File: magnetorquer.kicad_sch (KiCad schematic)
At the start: 20 parts, among them J2 Conn_01x07_Female, SW1 SW_Push, U1 MSP430FR5994IPN, Y1 Crystal, Y2 DNP

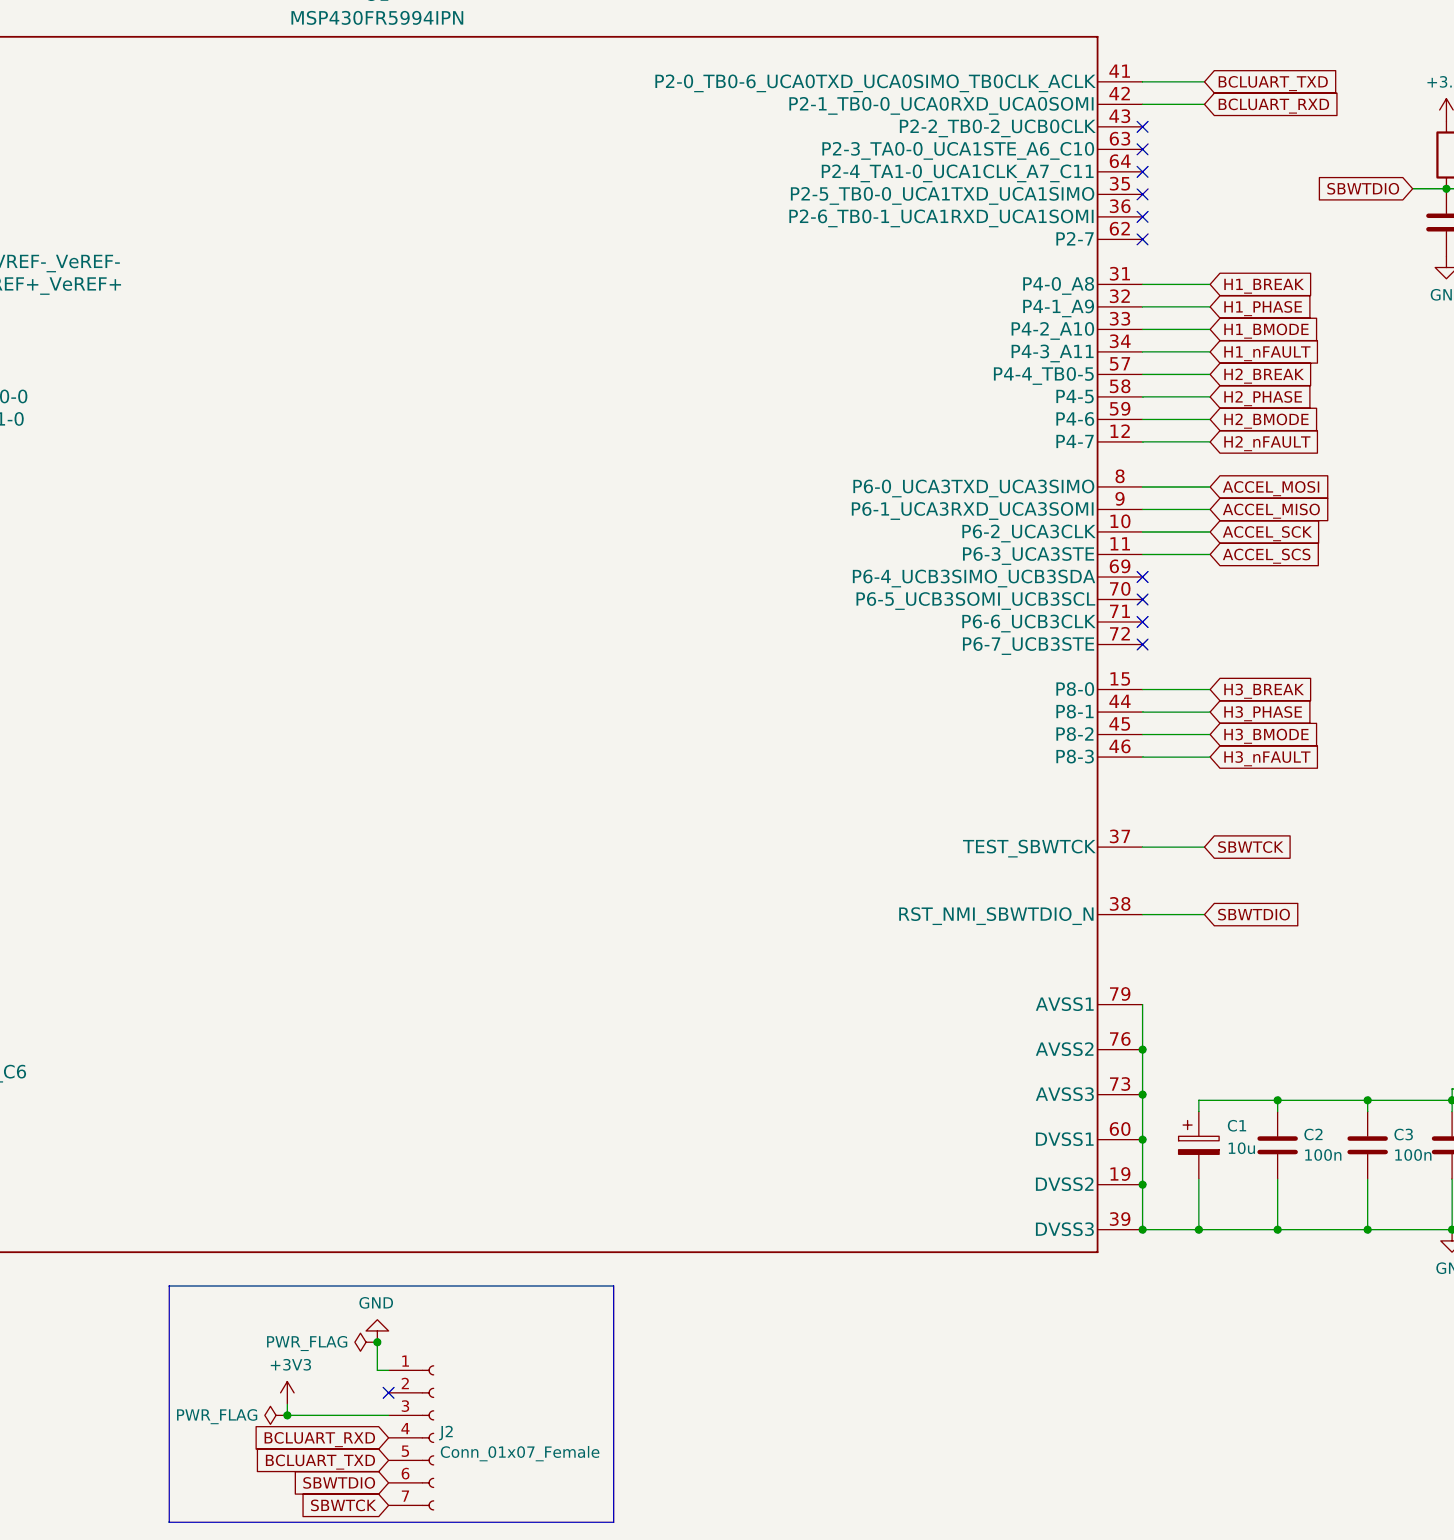
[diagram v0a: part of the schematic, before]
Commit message: schematic update hall sensor
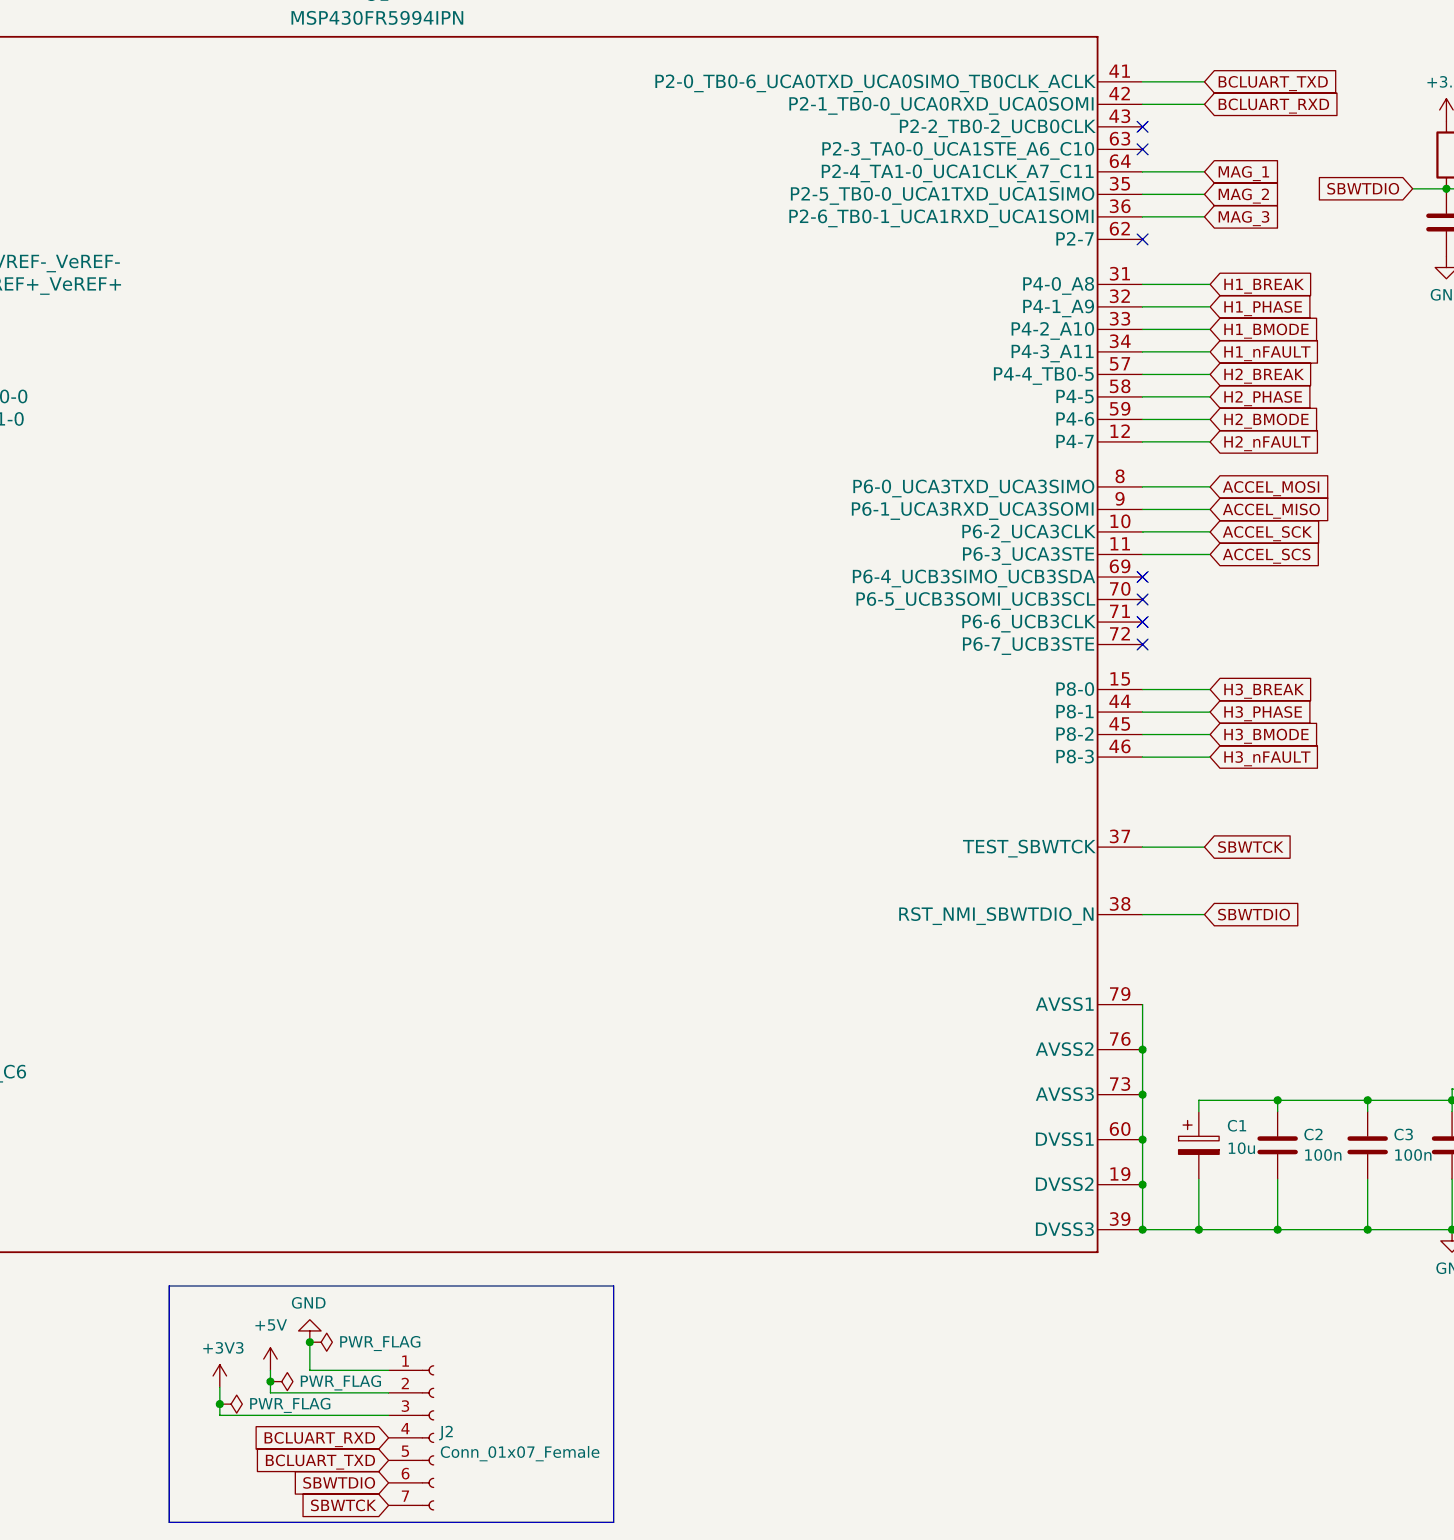
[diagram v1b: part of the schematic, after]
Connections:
- net MAG_2: now reaches U1.35 (P2-5_TB0-0_UCA1TXD_UCA1SIMO)
- net MAG_3: now reaches U1.36 (P2-6_TB0-1_UCA1RXD_UCA1SOMI)
- net MAG_1: now reaches U1.64 (P2-4_TA1-0_UCA1CLK_A7_C11)
- net +5V: now reaches J2.2 (Pin_2)
- no-connect marks 29 -> 25

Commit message: start layout
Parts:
- U1: footprint magnetorque_lib:MSP430FR5994IPM -> magnetorque_lib:MSP430FR5994IPN; symbol magnetorquer-rescue:MSP430FR5994IPN-msp -> msp:MSP430FR5994IPN
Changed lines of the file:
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@@
     )
   )
-  (symbol (lib_id "magnetorquer-rescue:MSP430FR5994IPN-msp") (at 144.145 93.98 0) (unit 1)
+  (symbol (lib_id "msp:MSP430FR5994IPN") (at 144.145 93.98 0) (unit 1)
     (in_bom yes) (on_board yes)
     (property "Reference" "U1" (id 0) (at 144.145 20.6248 0)
@@
       (effects (font (size 1.524 1.524)))
     )
-    (property "Footprint" "magnetorque_lib:MSP430FR5994IPM" (id 2) (at 144.145 95.504 0)
-      (effects (font (size 1.524 1.524)) hide)
+    (property "Footprint" "magnetorque_lib:MSP430FR5994IPN" (id 2) (at 144.145 95.504 0)
+      (effects (font (size 1.524 1.524)))
     )
     (property "Datasheet" "" (id 3) (at 144.145 93.98 0)
@@
     )
     (path "/00000000-0000-0000-0000-00006179e03e/fdcb2037-bdef-4a8f-9927-3cf386350a08"
-      (reference "L1") (unit 1) (value "L_Iron") (footprint "")
+      (reference "L1") (unit 1) (value "L_Iron") (footprint "magnetorque_lib:magnetorquer")
     )
     (path "/00000000-0000-0000-0000-00006179e03e/2085504c-bacb-4d13-8d16-341c091f40b1"
-      (reference "L2") (unit 1) (value "L_Iron") (footprint "")
+      (reference "L2") (unit 1) (value "L_Iron") (footprint "magnetorque_lib:magnetorquer")
     )
     (path "/00000000-0000-0000-0000-00006179e03e/e07af271-de8d-49c5-8d5e-0dfd6ae788f6"
-      (reference "L3") (unit 1) (value "L_Iron") (footprint "")
+      (reference "L3") (unit 1) (value "L_Iron") (footprint "magnetorque_lib:magnetorquer")
     )
     (path "/00000000-0000-0000-0000-00006166ef94"
@@
     )
     (path "/00000000-0000-0000-0000-0000615e437b"
-      (reference "U1") (unit 1) (value "MSP430FR5994IPN") (footprint "magnetorque_lib:MSP430FR5994IPM")
+      (reference "U1") (unit 1) (value "MSP430FR5994IPN") (footprint "magnetorque_lib:MSP430FR5994IPN")
     )
     (path "/00000000-0000-0000-0000-00006179e03e/00000000-0000-0000-0000-0000617b4502"

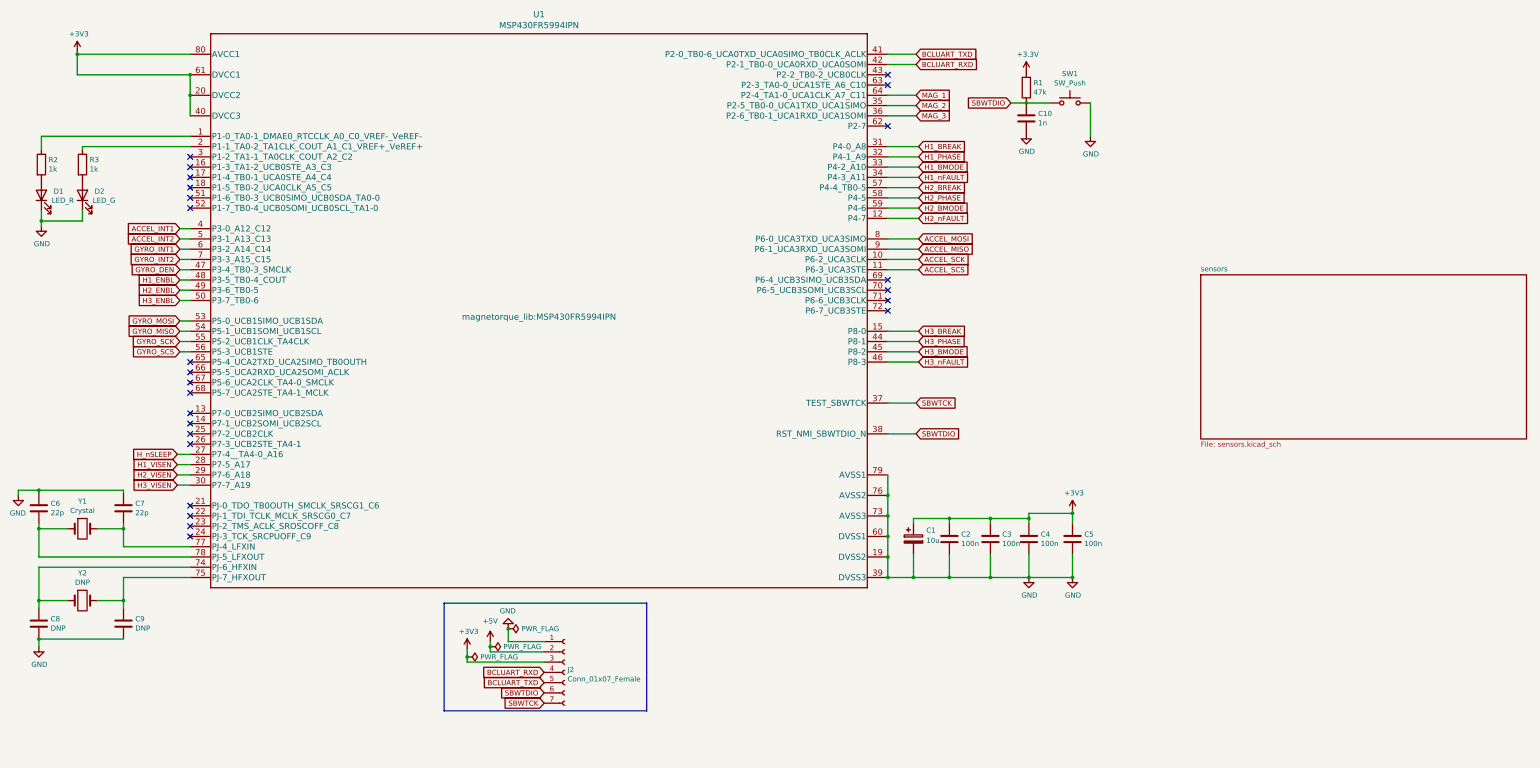
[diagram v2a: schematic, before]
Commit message: adicionado conector pc104
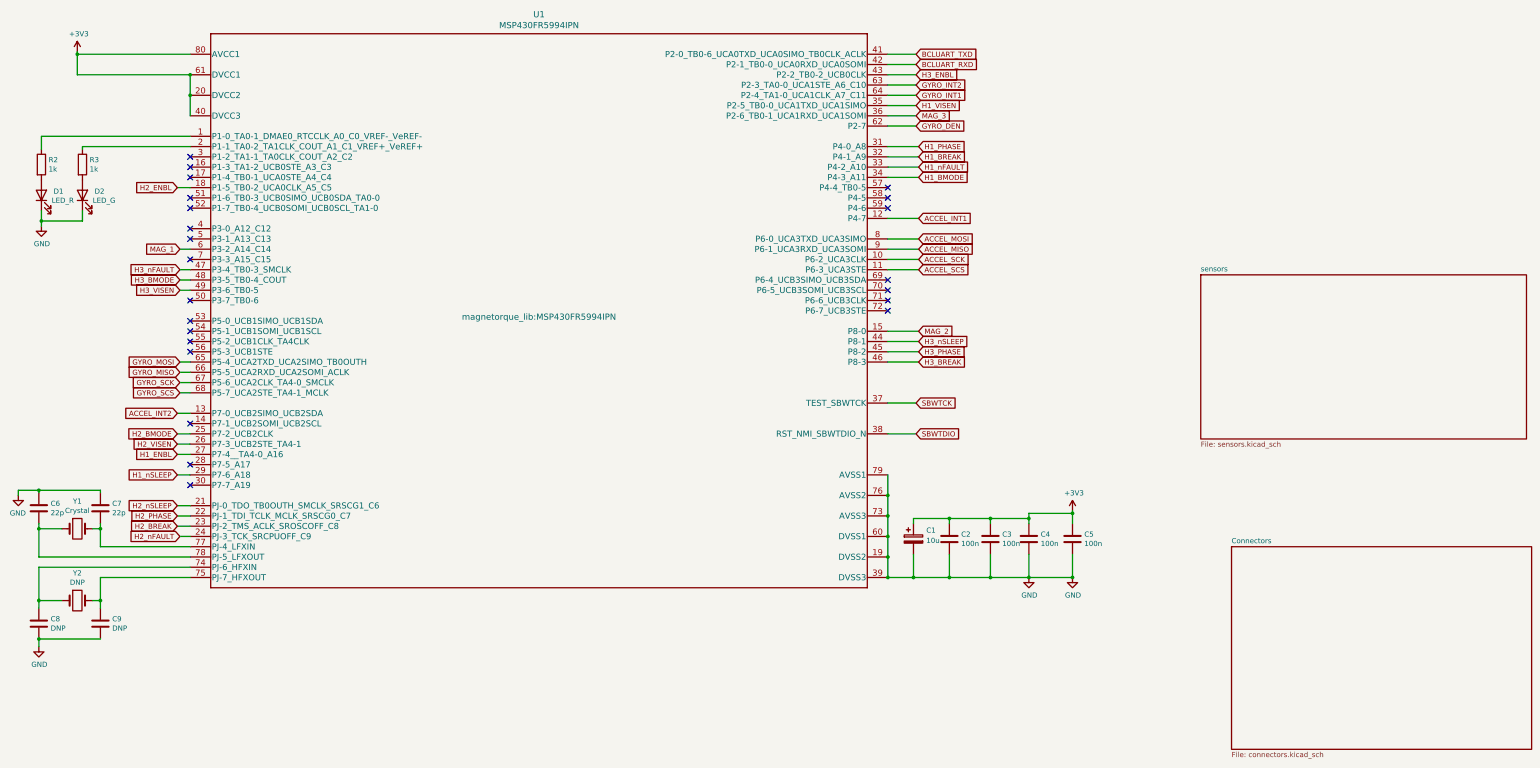
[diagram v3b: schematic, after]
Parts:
- removed C10: 1n, Capacitor_SMD:C_0805_2012Metric, symbol Device:C
- removed J2: Conn_01x07_Female, Connector_PinHeader_1.00mm:PinHeader_1x07_P1.00mm_Vertical, symbol Connector:Conn_01x07_Female
- removed R1: 47k, Resistor_SMD:R_0805_2012Metric, symbol Device:R
- removed SW1: SW_Push, Button_Switch_THT:SW_Tactile_Straight_KSL0Axx1LFTR, symbol Switch:SW_Push
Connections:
- net H_nSLEEP is gone; now on net H1_ENBL: U1.27 (P7-4__TA4-0_A16)
- net ACCEL_INT1: now also U1.12 (P4-7); no longer U1.4 (P3-0_A12_C12)
- net ACCEL_INT2: now also U1.13 (P7-0_UCB2SIMO_UCB2SDA); no longer U1.5 (P3-1_A13_C13)
- net GYRO_DEN: now also U1.62 (P2-7); no longer U1.47 (P3-4_TB0-3_SMCLK)
- net GYRO_INT1: now also U1.64 (P2-4_TA1-0_UCA1CLK_A7_C11); no longer U1.6 (P3-2_A14_C14)
- net GYRO_INT2: now also U1.63 (P2-3_TA0-0_UCA1STE_A6_C10); no longer U1.7 (P3-3_A15_C15)
- net GYRO_MISO: now also U1.66 (P5-5_UCA2RXD_UCA2SOMI_ACLK); no longer U1.54 (P5-1_UCB1SOMI_UCB1SCL)
- net GYRO_MOSI: now also U1.65 (P5-4_UCA2TXD_UCA2SIMO_TB0OUTH); no longer U1.53 (P5-0_UCB1SIMO_UCB1SDA)
- net GYRO_SCK: now also U1.67 (P5-6_UCA2CLK_TA4-0_SMCLK); no longer U1.55 (P5-2_UCB1CLK_TA4CLK)
- net GYRO_SCS: now also U1.68 (P5-7_UCA2STE_TA4-1_MCLK); no longer U1.56 (P5-3_UCB1STE)
- net H1_BMODE: now also U1.34 (P4-3_A11); no longer U1.33 (P4-2_A10)
- net H1_BREAK: now also U1.32 (P4-1_A9); no longer U1.31 (P4-0_A8)
- net H1_ENBL: no longer U1.48 (P3-5_TB0-4_COUT)
- net H1_PHASE: now also U1.31 (P4-0_A8); no longer U1.32 (P4-1_A9)
- net H1_VISEN: now also U1.35 (P2-5_TB0-0_UCA1TXD_UCA1SIMO); no longer U1.28 (P7-5_A17)
- net H1_nFAULT: now also U1.33 (P4-2_A10); no longer U1.34 (P4-3_A11)
- net H2_BMODE: now also U1.25 (P7-2_UCB2CLK); no longer U1.59 (P4-6)
- net H2_BREAK: now also U1.23 (PJ-2_TMS_ACLK_SROSCOFF_C8); no longer U1.57 (P4-4_TB0-5)
- net H2_ENBL: now also U1.18 (P1-5_TB0-2_UCA0CLK_A5_C5); no longer U1.49 (P3-6_TB0-5)
- net H2_PHASE: now also U1.22 (PJ-1_TDI_TCLK_MCLK_SRSCG0_C7); no longer U1.58 (P4-5)
- net H2_VISEN: now also U1.26 (P7-3_UCB2STE_TA4-1); no longer U1.29 (P7-6_A18)
- net H2_nFAULT: now also U1.24 (PJ-3_TCK_SRCPUOFF_C9); no longer U1.12 (P4-7)
- net H3_BMODE: now also U1.48 (P3-5_TB0-4_COUT); no longer U1.45 (P8-2)
- net H3_BREAK: now also U1.46 (P8-3); no longer U1.15 (P8-0)
- net H3_ENBL: now also U1.43 (P2-2_TB0-2_UCB0CLK); no longer U1.50 (P3-7_TB0-6)
- net H3_PHASE: now also U1.45 (P8-2); no longer U1.44 (P8-1)
- net H3_VISEN: now also U1.49 (P3-6_TB0-5); no longer U1.30 (P7-7_A19)
- net H3_nFAULT: now also U1.47 (P3-4_TB0-3_SMCLK); no longer U1.46 (P8-3)
- net MAG_1: now also U1.6 (P3-2_A14_C14); no longer U1.64 (P2-4_TA1-0_UCA1CLK_A7_C11)
- net MAG_2: now also U1.15 (P8-0); no longer U1.35 (P2-5_TB0-0_UCA1TXD_UCA1SIMO)
- net H2_nSLEEP: now reaches U1.21 (PJ-0_TDO_TB0OUTH_SMCLK_SRSCG1_C6)
- new net H1_nSLEEP: U1.29 (P7-6_A18)
- new net H3_nSLEEP: U1.44 (P8-1)
- no-connect marks 25 -> 23
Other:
- added sheet Connectors (connectors.kicad_sch)
- moved on the sheet: C7, C9, Y1, Y2

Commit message: last commit
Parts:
- removed C8, C9: DNP, Capacitor_SMD:C_0805_2012Metric, symbol Device:C
- removed Y2: DNP, Crystal:Crystal_HC49-4H_Vertical, symbol Device:Crystal
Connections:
- net H1_BMODE: no longer names the net of U1.34 (P4-3_A11)
- net H1_BREAK renamed H1_IN2
- net H1_ENBL: no longer names the net of U1.27 (P7-4__TA4-0_A16)
- net H1_PHASE renamed H1_IN1
- net H1_VISEN: no longer names the net of U1.35 (P2-5_TB0-0_UCA1TXD_UCA1SIMO)
- net H1_nFAULT: no longer names the net of U1.33 (P4-2_A10)
- net H1_nSLEEP renamed H_nSLEEP
- net H2_BMODE renamed H2_IN1
- net H2_BREAK: no longer names the net of U1.23 (PJ-2_TMS_ACLK_SROSCOFF_C8)
- net H2_ENBL: no longer names the net of U1.18 (P1-5_TB0-2_UCA0CLK_A5_C5)
- net H2_PHASE: no longer names the net of U1.22 (PJ-1_TDI_TCLK_MCLK_SRSCG0_C7)
- net H2_VISEN renamed H2_IN2
- net H2_nFAULT: no longer names the net of U1.24 (PJ-3_TCK_SRCPUOFF_C9)
- net H2_nSLEEP: no longer names the net of U1.21 (PJ-0_TDO_TB0OUTH_SMCLK_SRSCG1_C6)
- net H3_BMODE renamed H3_IN1
- net H3_BREAK: no longer names the net of U1.46 (P8-3)
- net H3_ENBL: no longer names the net of U1.43 (P2-2_TB0-2_UCB0CLK)
- net H3_PHASE: no longer names the net of U1.45 (P8-2)
- net H3_VISEN renamed H3_IN2
- net H3_nFAULT: no longer names the net of U1.47 (P3-4_TB0-3_SMCLK)
- net H3_nSLEEP: no longer names the net of U1.44 (P8-1)
- net MAG_3: no longer names the net of U1.36 (P2-6_TB0-1_UCA1RXD_UCA1SOMI)
- no-connect marks 23 -> 40
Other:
- added sheet coils (coils.kicad_sch)
